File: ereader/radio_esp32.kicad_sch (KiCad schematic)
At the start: 36 parts, among them U25 TXU0102DCUR, U27 TXU0202DCUR, U3 ESP32-C6-WROOM-1-N8, U4 TPS22964CYZPT, U5 TXU0304PWR, U6 TPS389001DSET, U7 SN74LVC1G97DBVR, U8 SN74LVC1G97DBVR

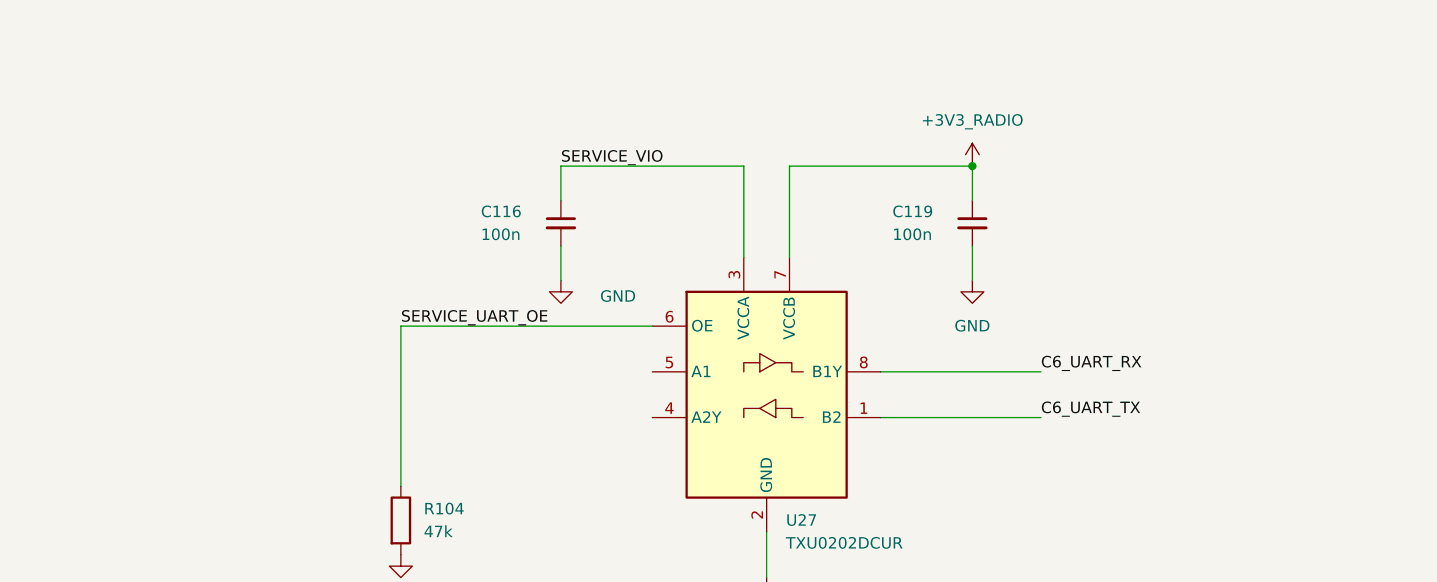
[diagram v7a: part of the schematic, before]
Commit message: Add service UART output pull-ups and refresh schematic PDF
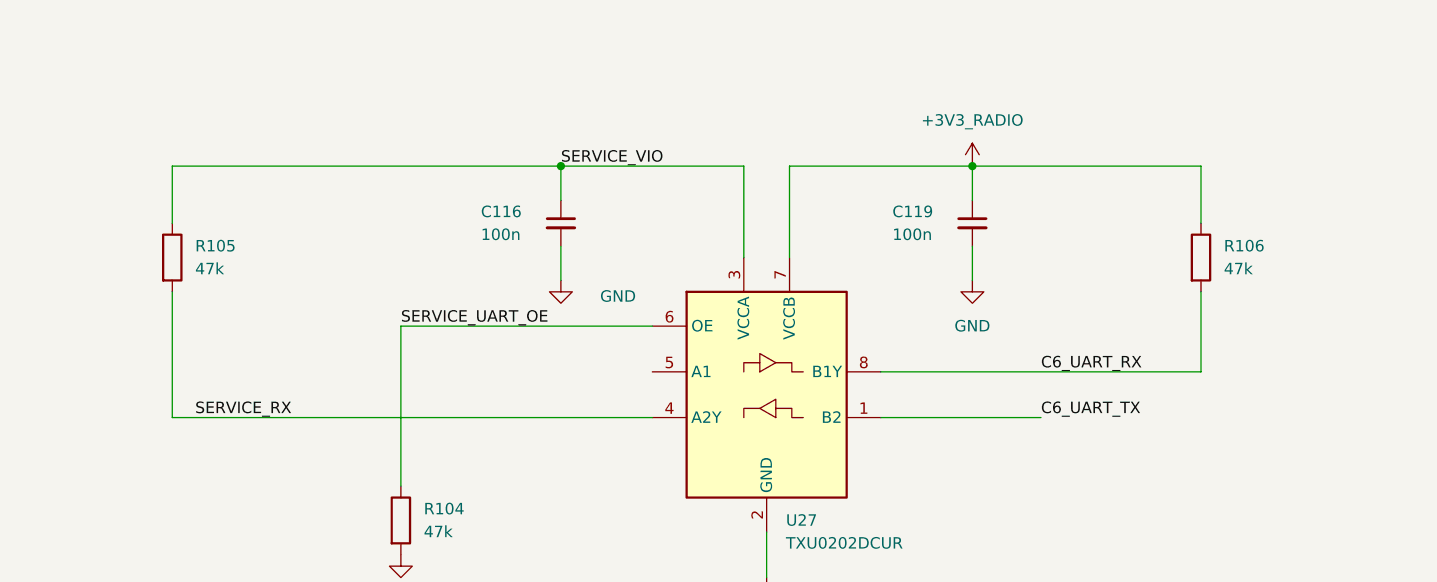
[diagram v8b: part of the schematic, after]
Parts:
- added R105, R106: 47k, symbol Device:R
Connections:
- net +3V3_RADIO: now also R106.1
- net C6_UART_RX: now also R106.2
- net SERVICE_VIO: now also R105.1
- net SERVICE_RX: now reaches U27.4 (A2Y)
- net SERVICE_RX: now also R105.2
